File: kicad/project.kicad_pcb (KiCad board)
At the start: 2 copper layers, 23 parts, among them J1 SWD, U1 STM32L031F4Px

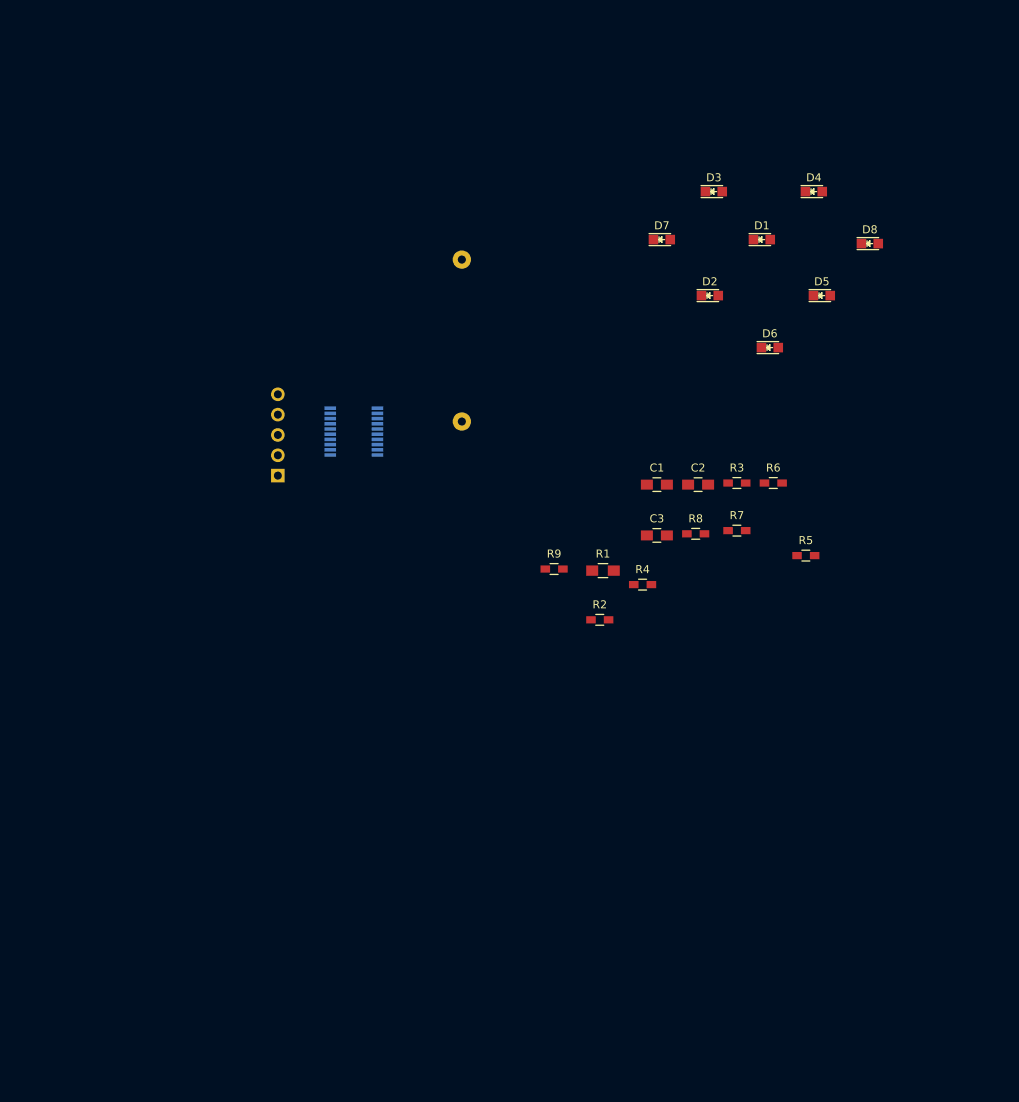
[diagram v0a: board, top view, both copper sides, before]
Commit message: 7 leds on individual pwm
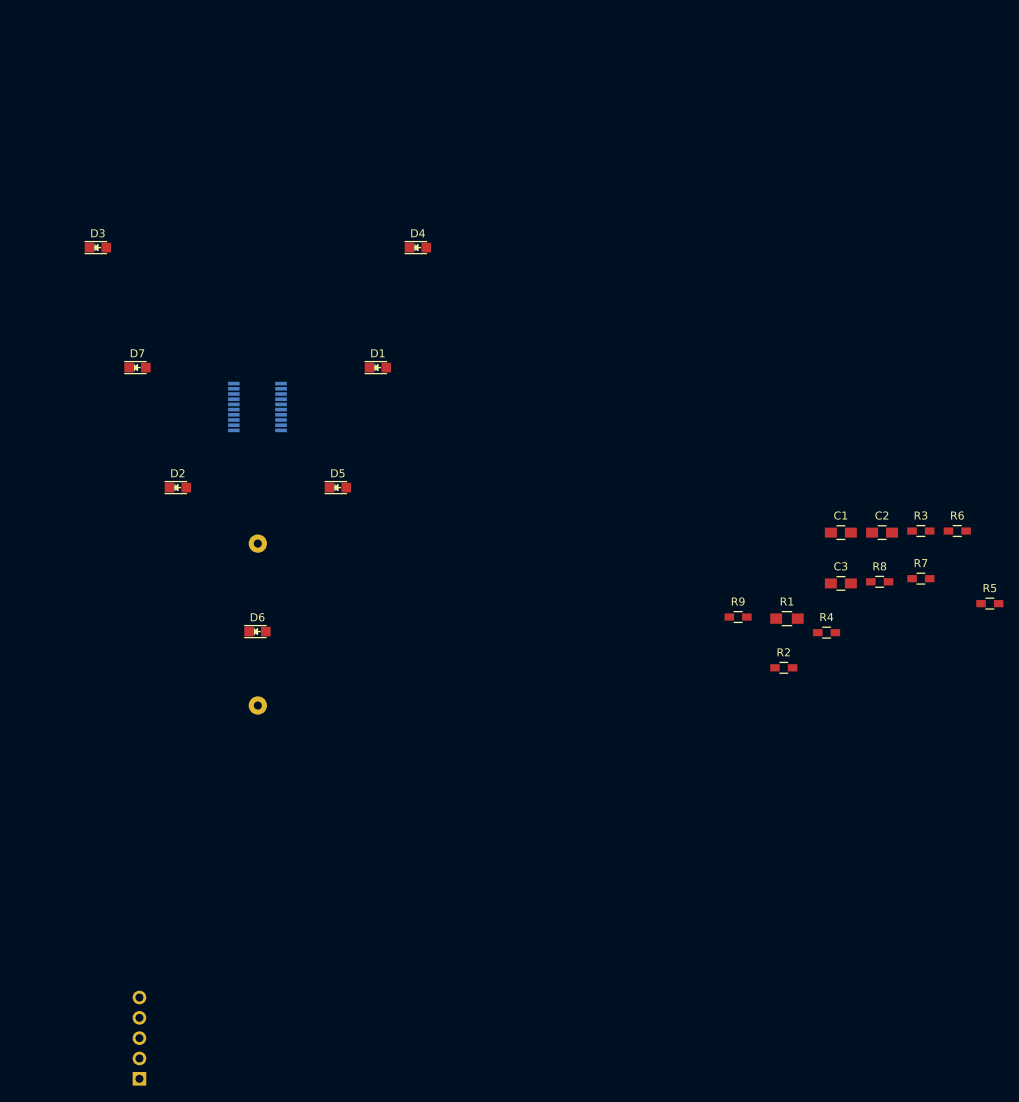
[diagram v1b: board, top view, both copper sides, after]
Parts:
- removed D8: LED, LEDs:LED_0805
- moved J1 77.4 mm to (115.2, 183.9)
- moved D3 77.3 mm to (110.0, 80.0)
- moved D6 73.2 mm to (130.0, 128.0)
- moved D2 70.7 mm to (120.0, 110.0)
- moved D7 67.5 mm to (115.0, 95.0)
- moved D5 65.1 mm to (140.0, 110.0)
- moved D1 50.6 mm to (145.0, 95.0)
- moved D4 50.0 mm to (150.0, 80.0)
- moved BT1 43.7 mm to (130.0, 122.0)
- moved C1 23.8 mm to (202.9, 115.6)
- moved C2 23.8 mm to (208.0, 115.6)
- moved C3 23.8 mm to (202.9, 122.0)
- moved R1 23.8 mm to (196.1, 126.4)
- moved R2 23.8 mm to (195.7, 132.5)
- moved R3 23.8 mm to (212.9, 115.4)
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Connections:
- U1 pad 10: Net-(R6-Pad2) -> Net-(U1-Pad10)
- U1 pad 11: Net-(R7-Pad2) -> Net-(R5-Pad2)
- U1 pad 12: Net-(R8-Pad2) -> Net-(R6-Pad2)
- U1 pad 13: Net-(R9-Pad2) -> Net-(R7-Pad2)
- U1 pad 14: Net-(U1-Pad14) -> Net-(R8-Pad2)
- U1 pad 6: Net-(R2-Pad2) -> Net-(U1-Pad6)
- U1 pad 7: Net-(R3-Pad2) -> Net-(R2-Pad2)
- U1 pad 8: Net-(R4-Pad2) -> Net-(R3-Pad2)
- U1 pad 9: Net-(R5-Pad2) -> Net-(R4-Pad2)

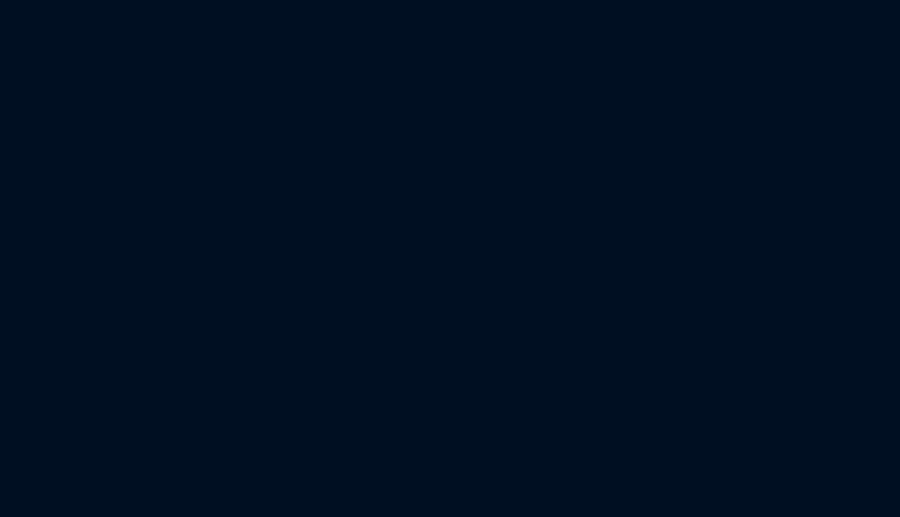
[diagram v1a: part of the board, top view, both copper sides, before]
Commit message: Power switch
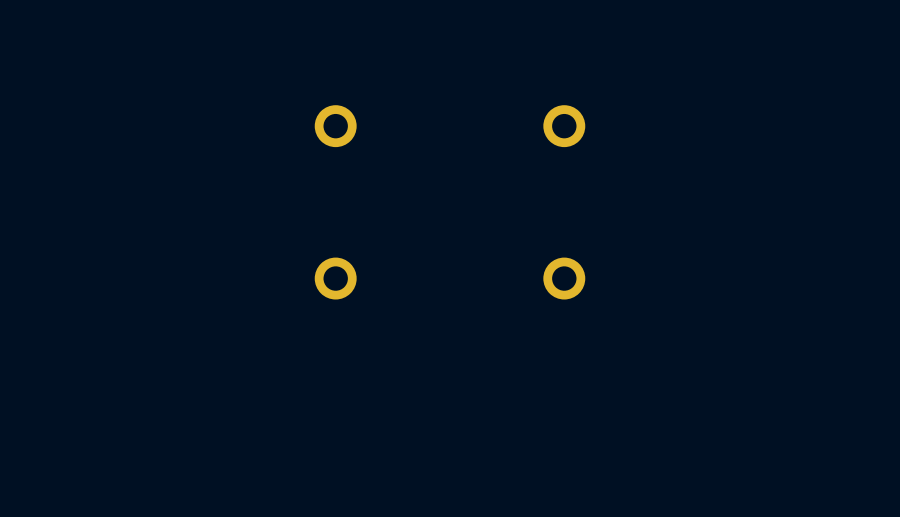
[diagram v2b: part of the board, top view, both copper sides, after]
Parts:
- added SW1: SW_SPST, Buttons_Switches_THT:SW_Tactile_Straight_KSA0Axx1LFTR, B.Cu at (126.0, 84.5)
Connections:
- BT1 pad 1: +BATT -> Net-(BT1-Pad1)
- C1 pad 1: +BATT -> Net-(BT1-Pad1)
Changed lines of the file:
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@@
-(kicad_pcb (version 4) (host pcbnew 4.0.7-e2-6376~58~ubuntu16.04.1)
+(kicad_pcb (version 4) (host pcbnew 4.0.6)
   (general
-    (links 37)
-    (no_connects 37)
+    (links 40)
+    (no_connects 40)
     (area 0 0 0 0)
     (thickness 1.6)
@@
     (tracks 0)
     (zones 0)
-    (modules 22)
-    (nets 29)
+    (modules 23)
+    (nets 30)
   )
   (page A4)
@@
   (net 27 "Net-(U1-Pad6)")
   (net 28 "Net-(U1-Pad10)")
+  (net 29 "Net-(BT1-Pad1)")
   (net_class Default "This is the default net class."
     (clearance 0.2032)
@@
     (add_net GND)
     (add_net NRST)
+    (add_net "Net-(BT1-Pad1)")
     (add_net "Net-(D1-Pad2)")
     (add_net "Net-(D2-Pad2)")
@@
     (fp_line (start -0.5 0.85) (end 0.5 0.85) (layer F.SilkS) (width 0.15))
     (pad 1 smd rect (at -1.25 0) (size 1.5 1.25) (layers F.Cu F.Paste F.Mask)
-      (net 1 +BATT))
+      (net 29 "Net-(BT1-Pad1)"))
     (pad 2 smd rect (at 1.25 0) (size 1.5 1.25) (layers F.Cu F.Paste F.Mask)
       (net 2 GND))
@@
       (net 2 GND))
     (pad 1 thru_hole circle (at 15.24 0 270) (size 2.286 2.286) (drill 1.016) (layers *.Cu *.Mask B.SilkS)
+      (net 29 "Net-(BT1-Pad1)"))
+  )
+  (module Buttons_Switches_THT:SW_Tactile_Straight_KSA0Axx1LFTR (layer B.Cu)
+    (at 126 84.5)
+    (descr "SW PUSH SMALL http://www.ckswitches.com/media/1457/ksa_ksl.pdf")
+    (tags "SW PUSH SMALL Tactile C&K")
+    (fp_text reference SW1 (at 3.81 2.08) (layer B.SilkS)
+      (effects (font (size 1 1) (thickness 0.15)) (justify mirror))
+    )
+    (fp_text value SW_SPST (at 3.81 -7.28) (layer B.Fab)
+      (effects (font (size 1 1) (thickness 0.15)) (justify mirror))
+    )
+    (fp_line (start 7.51 -6.24) (end 0.11 -6.24) (layer B.Fab) (width 0.1))
+    (fp_line (start 7.51 1.16) (end 7.51 -6.24) (layer B.Fab) (width 0.1))
+    (fp_line (start 0.11 1.16) (end 7.51 1.16) (layer B.Fab) (width 0.1))
+    (fp_line (start 0.11 -6.24) (end 0.11 1.16) (layer B.Fab) (width 0.1))
+    (fp_text user %R (at 3.81 -2.54) (layer B.Fab)
+      (effects (font (size 1 1) (thickness 0.15)) (justify mirror))
+    )
+    (fp_line (start 0 1.27) (end 7.62 1.27) (layer B.SilkS) (width 0.12))
+    (fp_line (start 7.62 1.27) (end 7.62 0.97) (layer B.SilkS) (width 0.12))
+    (fp_line (start 7.62 -6.35) (end 0 -6.35) (layer B.SilkS) (width 0.12))
+    (fp_line (start 0 1.27) (end 0 0.97) (layer B.SilkS) (width 0.12))
+    (fp_line (start 7.62 -0.97) (end 7.62 -4.11) (layer B.SilkS) (width 0.12))
+    (fp_line (start 0 -0.97) (end 0 -4.11) (layer B.SilkS) (width 0.12))
+    (fp_line (start -0.95 1.41) (end 8.57 1.41) (layer B.CrtYd) (width 0.05))
+    (fp_line (start -0.95 1.41) (end -0.95 -6.49) (layer B.CrtYd) (width 0.05))
+    (fp_line (start 8.57 -6.49) (end 8.57 1.41) (layer B.CrtYd) (width 0.05))
+    (fp_line (start 8.57 -6.49) (end -0.95 -6.49) (layer B.CrtYd) (width 0.05))
+    (fp_line (start 7.62 -6.05) (end 7.62 -6.35) (layer B.SilkS) (width 0.12))
+    (fp_line (start 0 -6.05) (end 0 -6.35) (layer B.SilkS) (width 0.12))
+    (fp_circle (center 3.81 -2.54) (end 3.81 0) (layer B.SilkS) (width 0.12))
+    (pad 1 thru_hole circle (at 7.62 0) (size 1.397 1.397) (drill 0.8128) (layers *.Cu *.Mask)
+      (net 29 "Net-(BT1-Pad1)"))
+    (pad 2 thru_hole circle (at 7.62 -5.08) (size 1.397 1.397) (drill 0.8128) (layers *.Cu *.Mask)
       (net 1 +BATT))
+    (pad 1 thru_hole circle (at 0 0) (size 1.397 1.397) (drill 0.8128) (layers *.Cu *.Mask)
+      (net 29 "Net-(BT1-Pad1)"))
+    (pad 2 thru_hole circle (at 0 -5.08) (size 1.397 1.397) (drill 0.8128) (layers *.Cu *.Mask)
+      (net 1 +BATT))
+    (model ${KISYS3DMOD}/Buttons_Switches_THT.3dshapes/SW_Tactile_Straight_KSA0Axx1LFTR.wrl
+      (at (xyz 0 0 0))
+      (scale (xyz 1 1 1))
+      (rotate (xyz 0 0 0))
+    )
   )
   (dimension 70 (width 0.3) (layer Cmts.User)

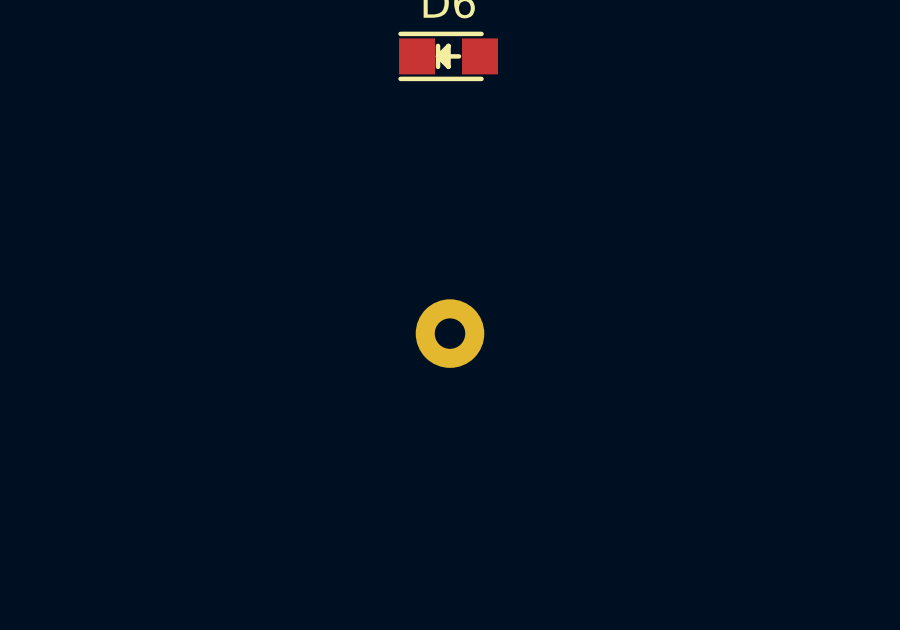
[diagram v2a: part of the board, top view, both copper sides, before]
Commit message: 19mm between legs of the battery holder
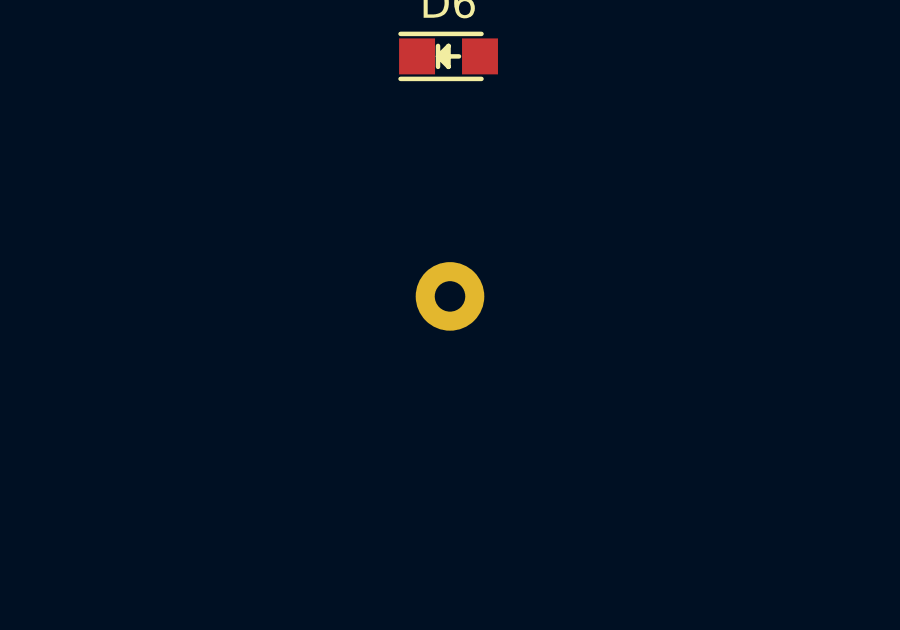
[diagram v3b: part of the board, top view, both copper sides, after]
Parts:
- BT1: footprint theapi:CR2032H -> CR2032H
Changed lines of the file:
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@@
-(kicad_pcb (version 4) (host pcbnew 4.0.6)
+(kicad_pcb (version 4) (host pcbnew 4.0.7-e2-6376~58~ubuntu16.04.1)
   (general
     (links 40)
     (no_connects 40)
-    (area 0 0 0 0)
+    (area 82.150001 57.3 223.779001 187.419)
     (thickness 1.6)
     (drawings 2)
@@
     (uvia_drill 0.1016)
   )
+  (module CR2032H (layer B.Cu)
+    (at 130 122 270)
+    (fp_text reference BT1 (at 0 12.7 270) (layer B.SilkS)
+      (effects (font (size 1 1) (thickness 0.15)) (justify mirror))
+    )
+    (fp_text value Battery_Cell (at 0 -12.7 270) (layer B.Fab)
+      (effects (font (size 1 1) (thickness 0.15)) (justify mirror))
+    )
+    (fp_arc (start 0 0) (end 7.62 7.62) (angle -90) (layer B.SilkS) (width 0.15))
+    (fp_arc (start 0 0) (end -7.62 -7.62) (angle -90) (layer B.SilkS) (width 0.15))
+    (fp_line (start 15.24 -3.81) (end 15.24 -5.08) (layer B.SilkS) (width 0.15))
+    (fp_line (start 14.605 -4.445) (end 15.875 -4.445) (layer B.SilkS) (width 0.15))
+    (fp_line (start 17.145 3.175) (end 17.78 3.175) (layer B.SilkS) (width 0.15))
+    (fp_line (start 17.78 3.175) (end 17.78 -3.175) (layer B.SilkS) (width 0.15))
+    (fp_line (start 17.78 -3.175) (end 17.145 -3.175) (layer B.SilkS) (width 0.15))
+    (fp_line (start 15.875 3.175) (end 17.145 3.175) (layer B.SilkS) (width 0.15))
+    (fp_line (start 17.145 -3.175) (end 10.795 -3.175) (layer B.SilkS) (width 0.15))
+    (fp_line (start 10.795 3.175) (end 15.875 3.175) (layer B.SilkS) (width 0.15))
+    (pad 2 thru_hole circle (at -5 0 270) (size 2.286 2.286) (drill 1.016) (layers *.Cu *.Mask B.SilkS)
+      (net 2 GND))
+    (pad 1 thru_hole circle (at 14 0 270) (size 2.286 2.286) (drill 1.016) (layers *.Cu *.Mask B.SilkS)
+      (net 29 "Net-(BT1-Pad1)"))
+  )
   (module Capacitors_SMD:C_0805_HandSoldering (layer F.Cu)
     (at 202.879001 115.629)
@@
     )
   )
-  (module theapi:CR2032H (layer B.Cu)
-    (at 130 122 270)
-    (fp_text reference BT1 (at 0 12.7 270) (layer B.SilkS)
-      (effects (font (size 1 1) (thickness 0.15)) (justify mirror))
-    )
-    (fp_text value Battery_Cell (at 0 -12.7 270) (layer B.Fab)
-      (effects (font (size 1 1) (thickness 0.15)) (justify mirror))
-    )
-    (fp_arc (start 0 0) (end 7.62 7.62) (angle -90) (layer B.SilkS) (width 0.15))
-    (fp_arc (start 0 0) (end -7.62 -7.62) (angle -90) (layer B.SilkS) (width 0.15))
-    (fp_line (start 15.24 -3.81) (end 15.24 -5.08) (layer B.SilkS) (width 0.15))
-    (fp_line (start 14.605 -4.445) (end 15.875 -4.445) (layer B.SilkS) (width 0.15))
-    (fp_line (start 17.145 3.175) (end 17.78 3.175) (layer B.SilkS) (width 0.15))
-    (fp_line (start 17.78 3.175) (end 17.78 -3.175) (layer B.SilkS) (width 0.15))
-    (fp_line (start 17.78 -3.175) (end 17.145 -3.175) (layer B.SilkS) (width 0.15))
-    (fp_line (start 15.875 3.175) (end 17.145 3.175) (layer B.SilkS) (width 0.15))
-    (fp_line (start 17.145 -3.175) (end 10.795 -3.175) (layer B.SilkS) (width 0.15))
-    (fp_line (start 10.795 3.175) (end 15.875 3.175) (layer B.SilkS) (width 0.15))
-    (pad 2 thru_hole circle (at -5 0 270) (size 2.286 2.286) (drill 1.016) (layers *.Cu *.Mask B.SilkS)
-      (net 2 GND))
-    (pad 1 thru_hole circle (at 15.24 0 270) (size 2.286 2.286) (drill 1.016) (layers *.Cu *.Mask B.SilkS)
-      (net 29 "Net-(BT1-Pad1)"))
-  )
   (module Buttons_Switches_THT:SW_Tactile_Straight_KSA0Axx1LFTR (layer B.Cu)

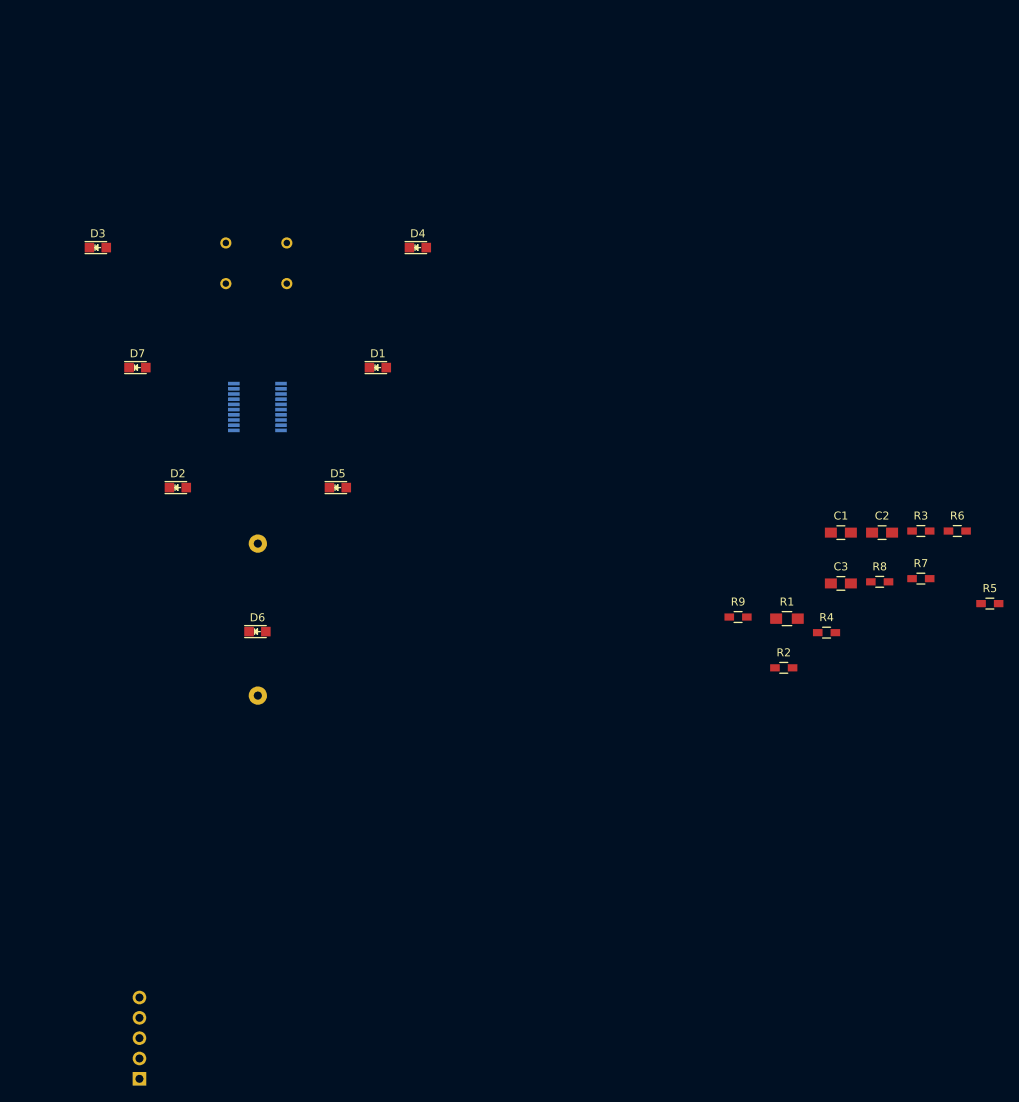
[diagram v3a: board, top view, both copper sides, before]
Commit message: 3 pin push switch
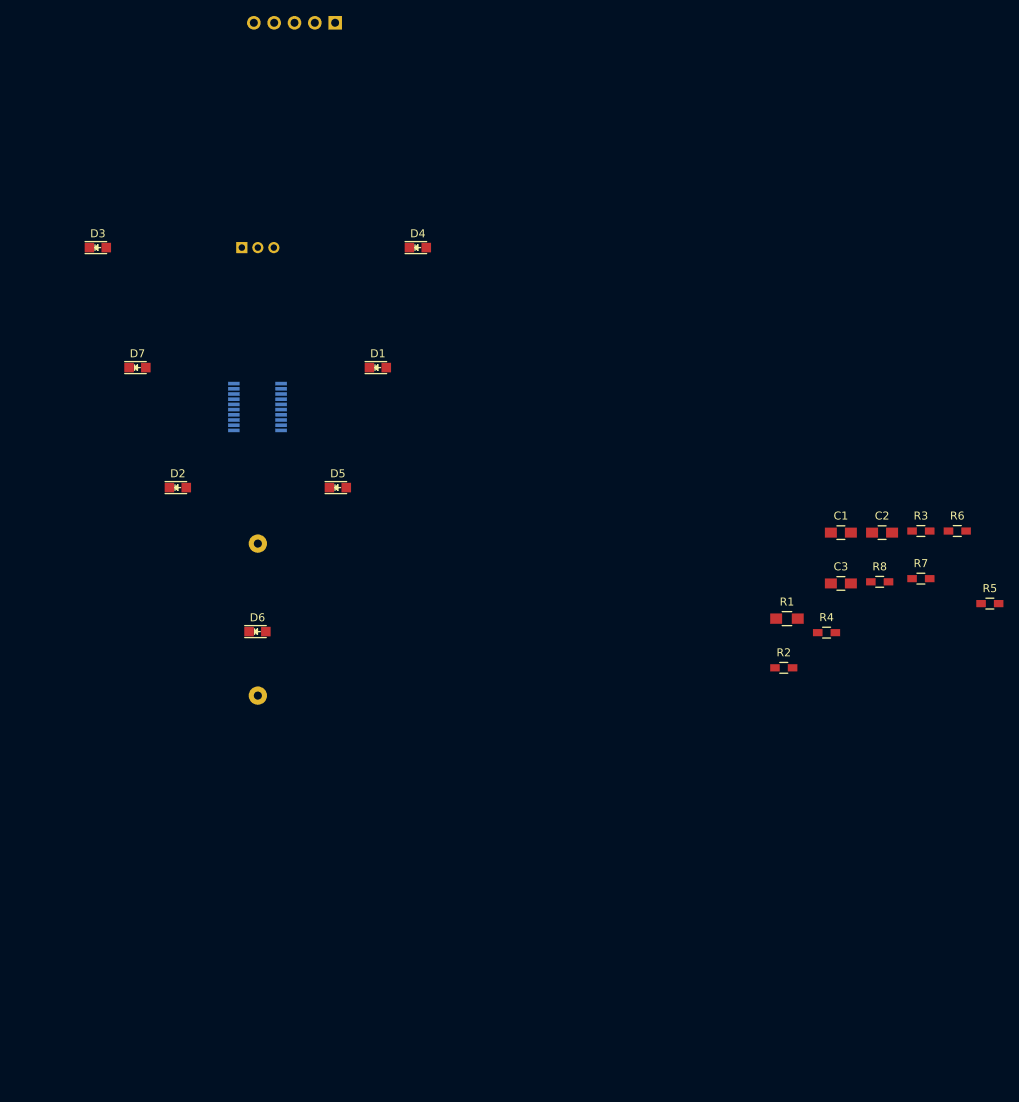
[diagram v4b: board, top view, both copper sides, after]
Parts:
- removed R9: 1k, Resistors_SMD:R_0603_HandSoldering
- BT1: footprint CR2032H -> theapi:CR2032H
- SW1: value SW_SPST -> SW_DPDT_x2; footprint Buttons_Switches_THT:SW_Tactile_Straight_KSA0Axx1LFTR -> SW_Micro_SPST
- moved J1 134.2 mm to (139.7, 51.9), turned to 90 degrees
- moved SW1 6.02 mm to (130.0, 80.0)
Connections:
- SW1 pad 1: Net-(BT1-Pad1) -> +BATT
- SW1 pad 2: +BATT -> Net-(BT1-Pad1)
